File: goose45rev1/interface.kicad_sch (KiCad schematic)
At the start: 13 parts, among them J1 USB_C_Receptacle_USB2.0, J2 SPI, J3 Debugger, J4 USB connector, J5 USART, U2 USBLC6-2SC6

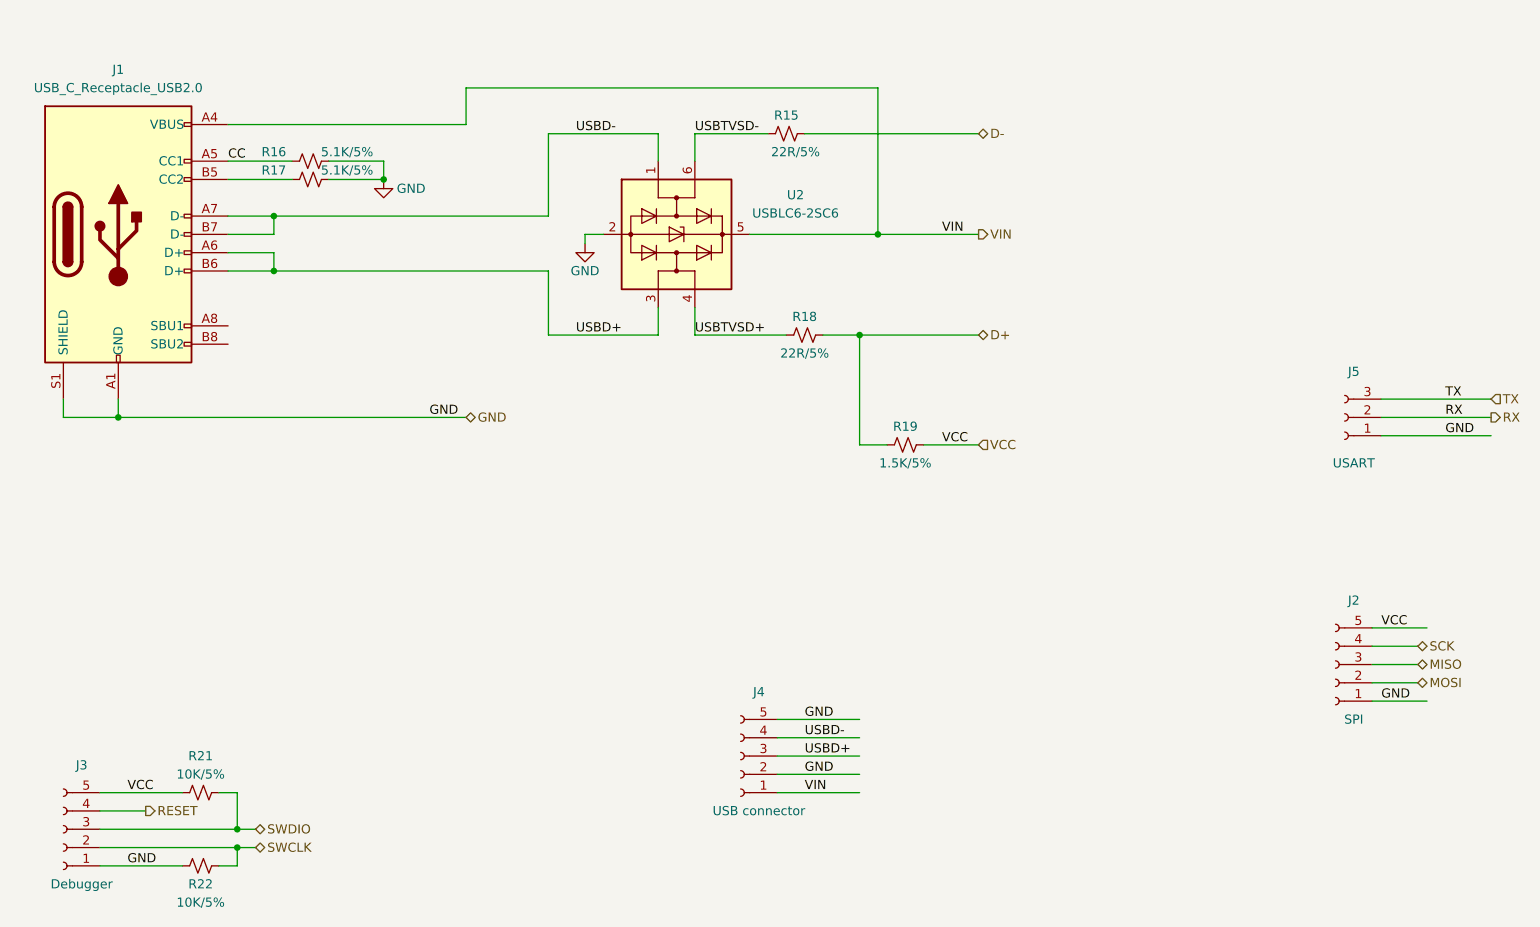
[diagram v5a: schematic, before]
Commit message: remove goose45 pcb usb type-c
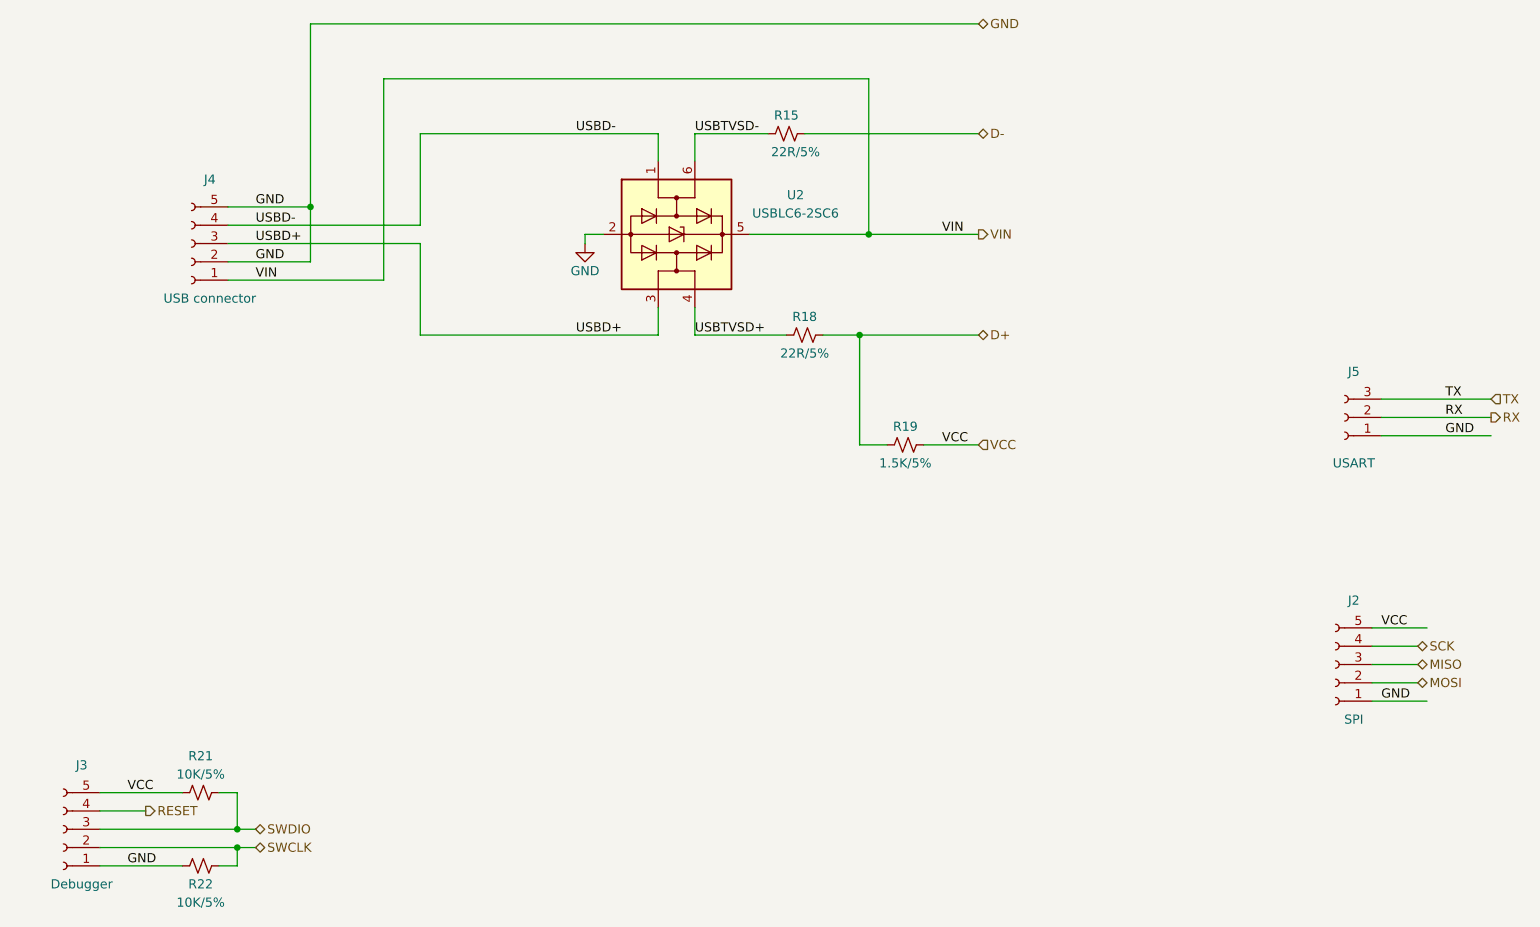
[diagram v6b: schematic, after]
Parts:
- removed J1: USB_C_Receptacle_USB2.0, Connector_USB:USB_C_Receptacle_HRO_TYPE-C-31-M-12, symbol Connector:USB_C_Receptacle_USB2.0
- removed R16, R17: 5.1K/5%, Resistor_SMD:R_0603_1608Metric, symbol Device:R_Small_US
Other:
- moved on the sheet: J4
